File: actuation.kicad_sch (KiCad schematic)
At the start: 23 parts

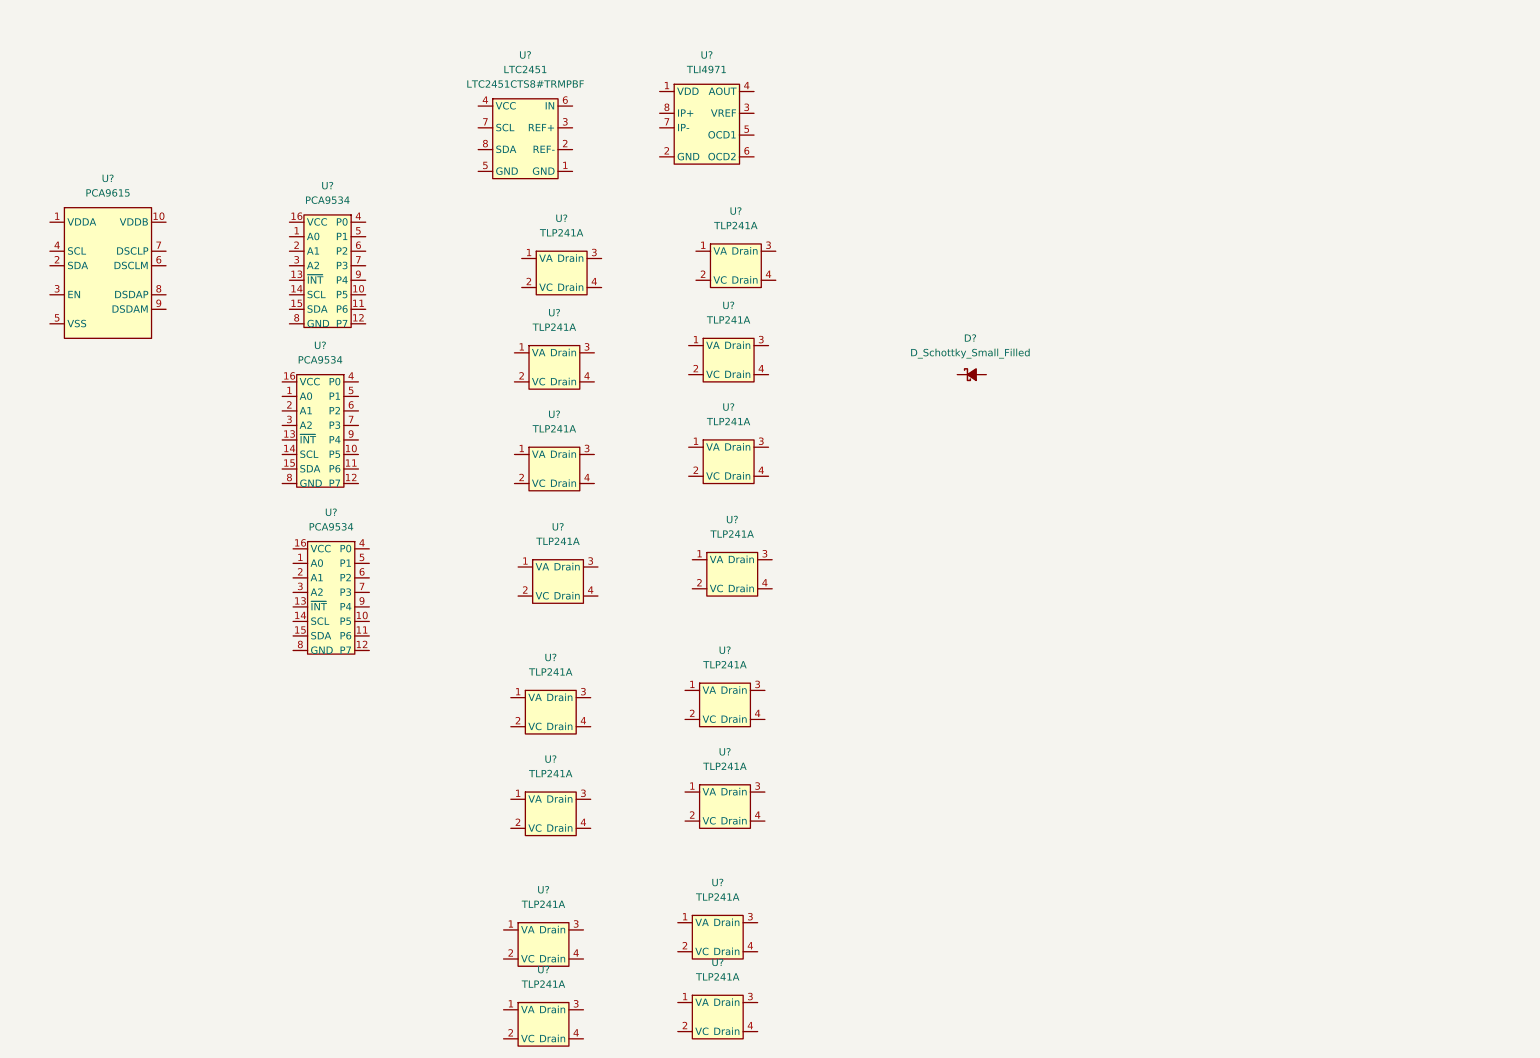
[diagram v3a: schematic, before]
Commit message: Worked on schematic, symbol placement weird
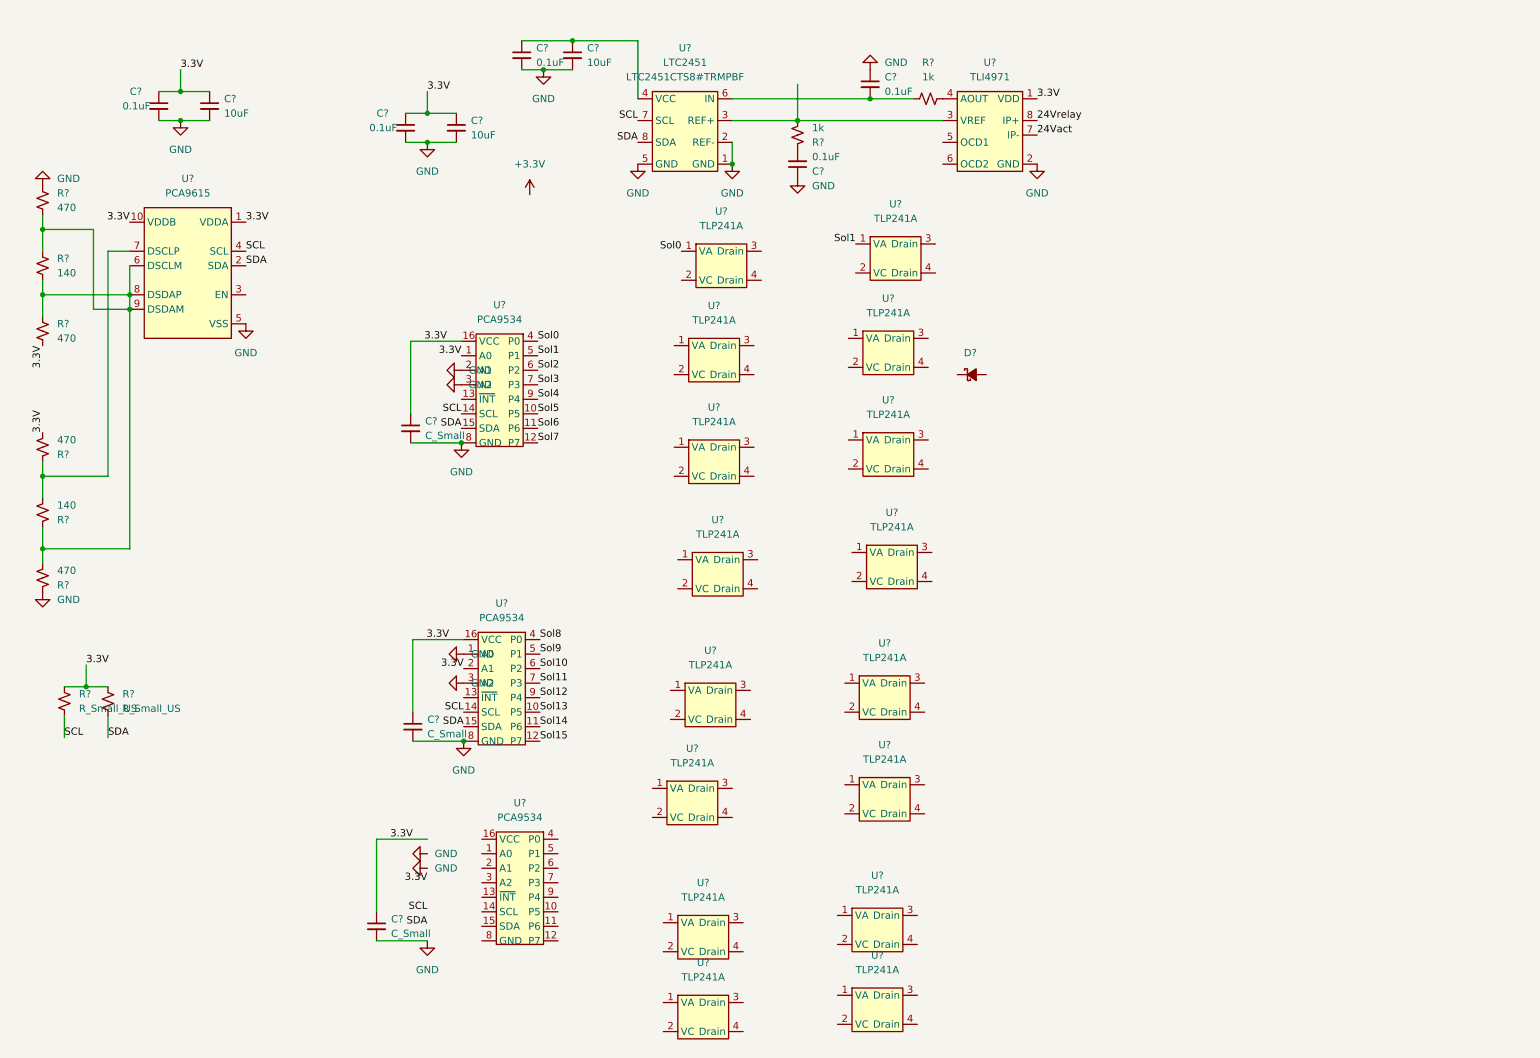
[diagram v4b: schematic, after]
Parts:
- removed U? (x2): PCA9534, Package_SO:TSSOP-16_4.4x5mm_P0.65mm, symbol actuation:PCA9534
- added C? (x3): 10uF, symbol Device:C_Small
- added C? (x5): 0.1uF, symbol Device:C_Small
- added C? (x3): C_Small, symbol Device:C_Small
- added R? (x4): 470, symbol Device:R_Small_US
- added R? (x2): 140, symbol Device:R_Small_US
- added R? (x2): 1k, symbol Device:R_Small_US
- added R? (x2): R_Small_US, symbol Device:R_Small_US
- added U? (x2): PCA9534, Package_SO:TSSOP-16_4.4x5mm_P0.65mm, symbol actuation:PCA9534
- D?: MPN (none) -> B2100A-13-F
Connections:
- net GND: now reaches U?.1 (GND)
- net GND: now also U?.2 (A1), U?.2 (GND), U?.2 (REF-), U?.3 (A2), U?.5 (GND), U?.5 (VSS), U?.8 (GND), C?.1, C?.1, C?.2, C?.2, C?.2, C?.2, C?.2, C?.2, C?.2, C?.2, C?.2, R?.2, R?.2, U?.1 (A0), U?.3 (A2), U?.8 (GND)
- net at U?.3 (REF+): now also U?.3 (VREF), R?.1
- net at U?.4 (VCC): now also C?.1, C?.1
- net at U?.6 (IN): now also C?.2, R?.1
- net SCL: now reaches U?.7 (SCL)
- net SCL: now also U?.14 (SCL), U?.4 (SCL), R?.2, U?.14 (SCL)
- net SDA: now reaches U?.8 (SDA)
- net SDA: now also U?.15 (SDA), U?.2 (SDA), R?.2, U?.15 (SDA)
- net Sol0: now reaches U?.1 (VA)
- net Sol0: now also U?.4 (P0)
- net 3.3V: now reaches U?.1 (VDD)
- net 3.3V: now also U?.1 (A0), U?.1 (VDDA), U?.10 (VDDB), U?.16 (VCC), C?.1, C?.1, C?.1, C?.1, C?.1, C?.1, C?.1, R?.1, R?.1, R?.1, R?.1, U?.16 (VCC), U?.2 (A1)
- net at U?.4 (AOUT): now also R?.2
- net 24Vact: now reaches U?.7 (IP-)
- net 24Vrelay: now reaches U?.8 (IP+)
- net Sol5: now reaches U?.10 (P5)
- net Sol6: now reaches U?.11 (P6)
- net Sol7: now reaches U?.12 (P7)
- net Sol1: now reaches U?.5 (P1)
- net Sol1: now also U?.1 (VA)
- net Sol2: now reaches U?.6 (P2)
- net Sol3: now reaches U?.7 (P3)
- net Sol4: now reaches U?.9 (P4)
- net at U?.6 (DSCLM): now also U?.8 (DSDAP), U?.9 (DSDAM), R?.1, R?.1, R?.1, R?.2, R?.2, R?.2
- net at U?.7 (DSCLP): now also R?.1, R?.2
- new net: C?.2, R?.2
- new net Sol10: U?.6 (P2)
- new net Sol11: U?.7 (P3)
- new net Sol12: U?.9 (P4)
- new net Sol13: U?.10 (P5)
- new net Sol14: U?.11 (P6)
- new net Sol15: U?.12 (P7)
- new net Sol8: U?.4 (P0)
- new net Sol9: U?.5 (P1)
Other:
- moved on the sheet: U?

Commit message: Added more symbols to schematic
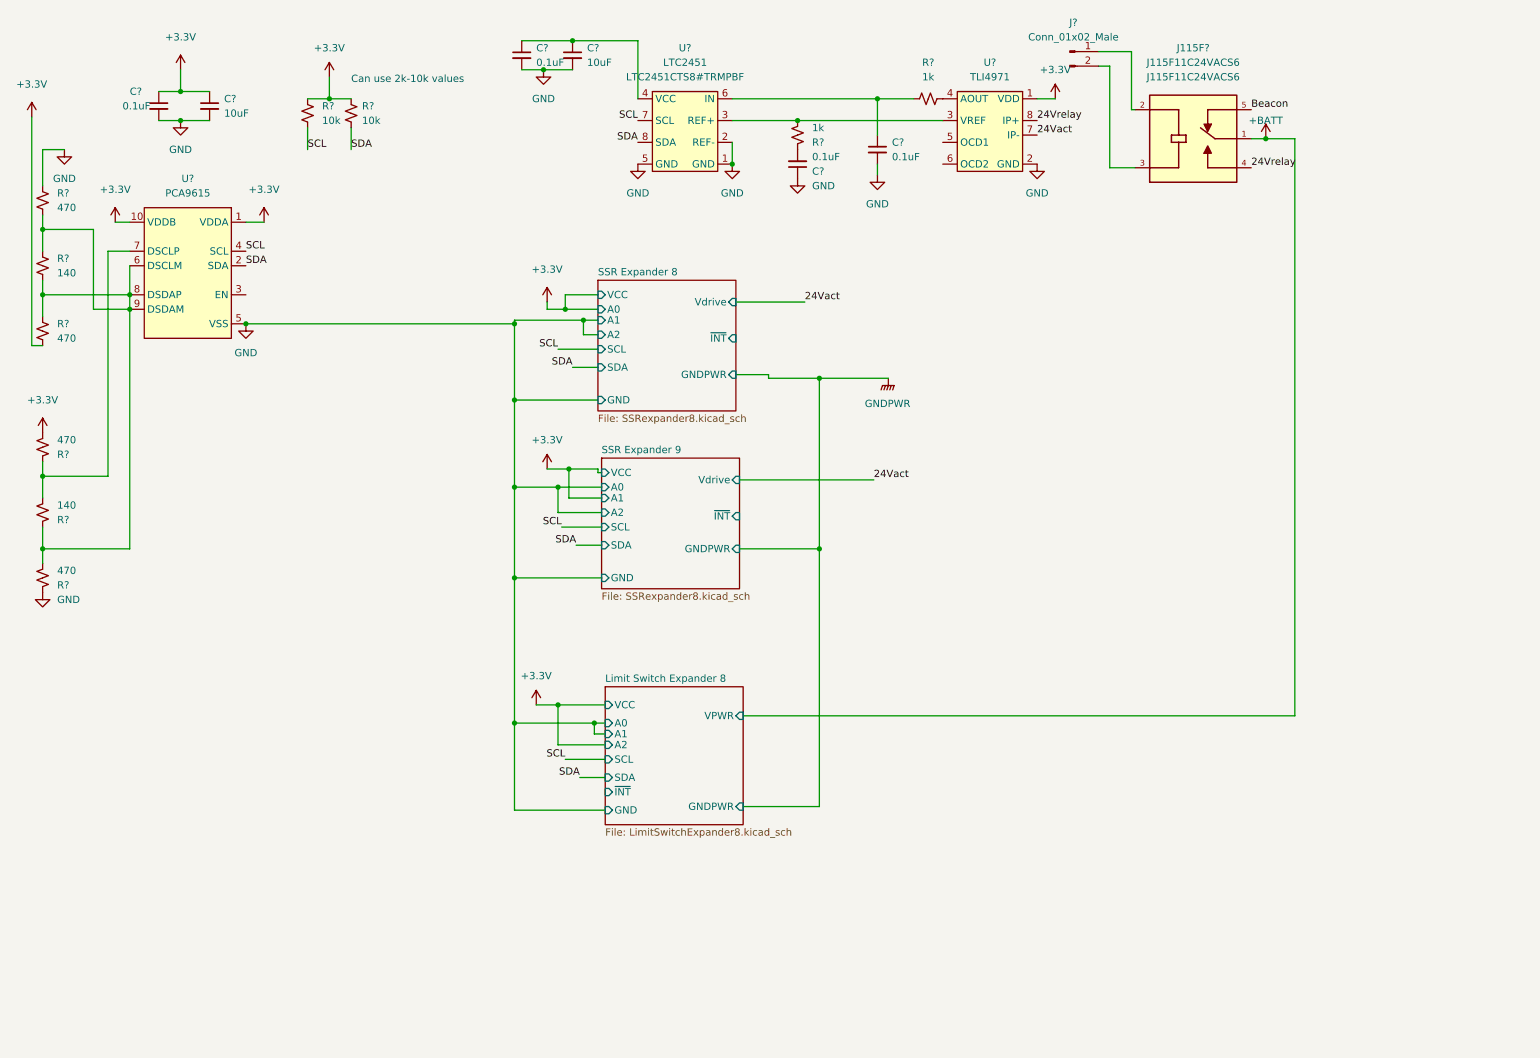
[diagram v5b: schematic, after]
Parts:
- removed C? (x2): 0.1uF, symbol Device:C_Small
- removed C?: 10uF, symbol Device:C_Small
- removed C? (x3): C_Small, symbol Device:C_Small
- removed D?: D_Schottky_Small_Filled, Diode_SMD:D_SMA, symbol Device:D_Schottky_Small_Filled
- removed U? (x16): TLP241A, symbol actuation:TLP241A
- removed U? (x3): PCA9534, Package_SO:TSSOP-16_4.4x5mm_P0.65mm, symbol actuation:PCA9534
- added C?: 0.1uF, symbol Device:C_Small
- added J115F?: J115F11C24VACS6, RELAY_J115F11C24VACS6, symbol actuation:J115F11C24VACS6
- added J?: Conn_01x02_Male, symbol Connector:Conn_01x02_Male
- R? (x2): value R_Small_US -> 10k
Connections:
- net 3.3V is gone; now on net +3.3V: C?.1, C?.1, R?.1, R?.1, R?.1, R?.1, U?.1 (VDD), U?.1 (VDDA), U?.10 (VDDB)
- net 24Vrelay: now also J115F?.4
- net GND: now also C?.2
- net at R?.1, U?.6 (IN): now also C?.1
- new net: J115F?.2, J?.1 (Pin_1)
- new net: J115F?.3, J?.2 (Pin_2)
- new net +BATT: J115F?.1
- new net Beacon: J115F?.5
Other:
- added sheet Limit Switch Expander 8 (LimitSwitchExpander8.kicad_sch)
- added sheet SSR Expander 8 (SSRexpander8.kicad_sch)
- added sheet SSR Expander 9 (SSRexpander8.kicad_sch)
- note added: "Can use 2k-10k values"
- moved on the sheet: R?

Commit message: Grid issues
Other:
- moved on the sheet: C?, J115F?, J?, R?, U?

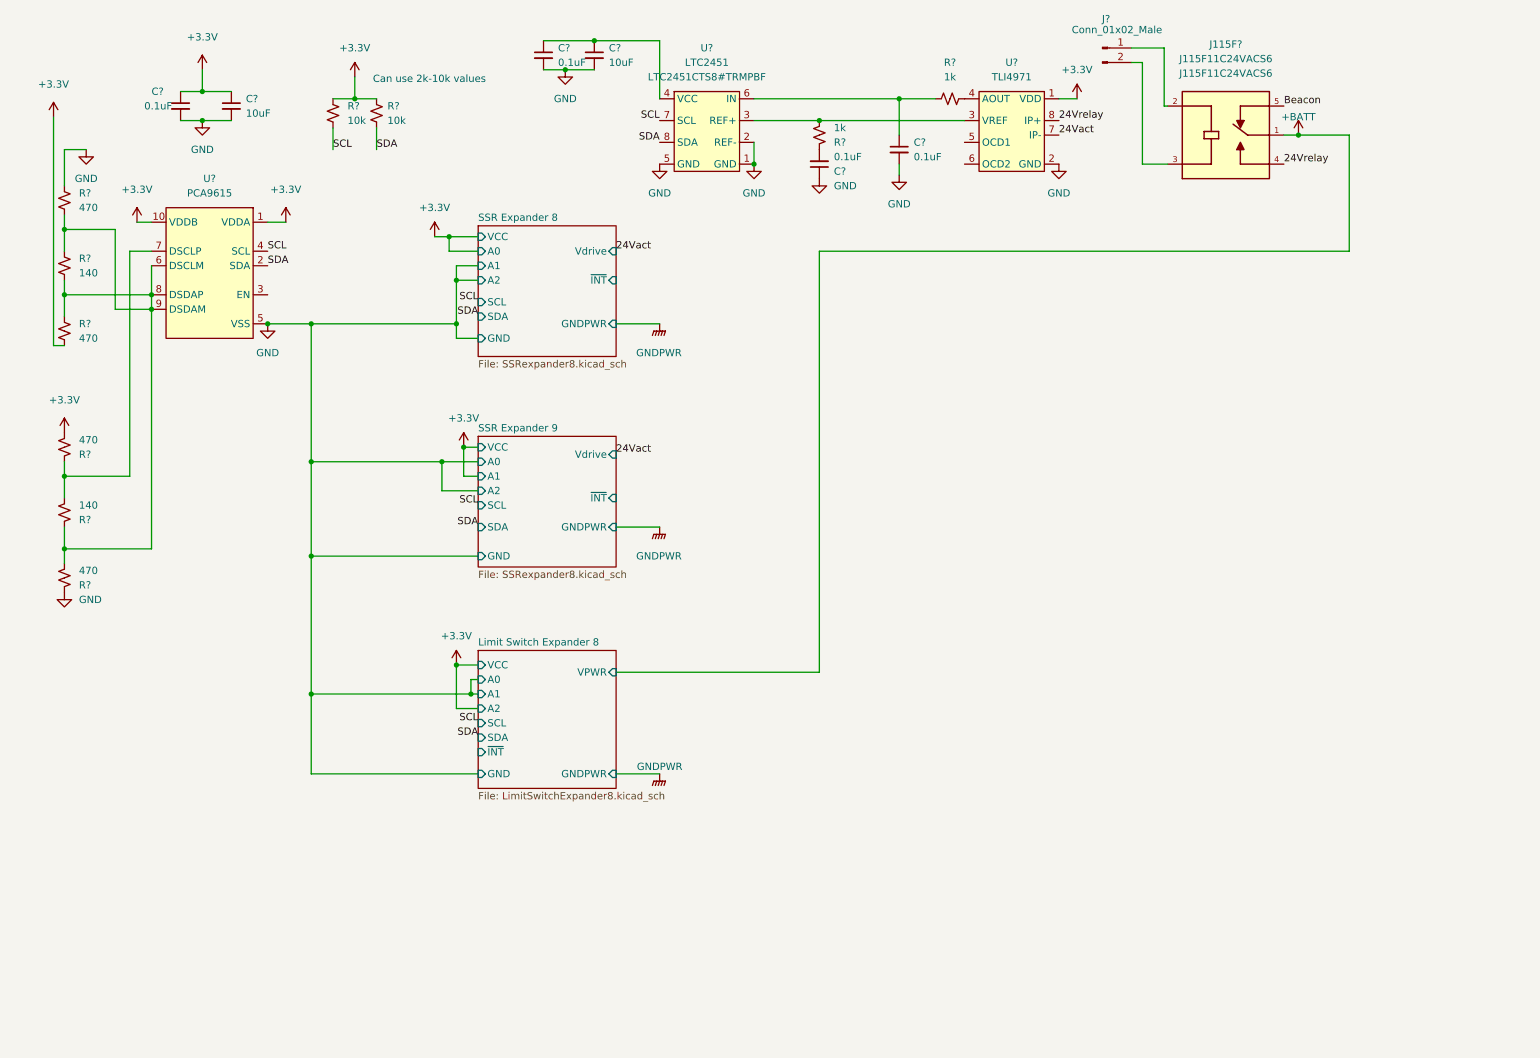
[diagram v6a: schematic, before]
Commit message: added db9 and 3.3buck
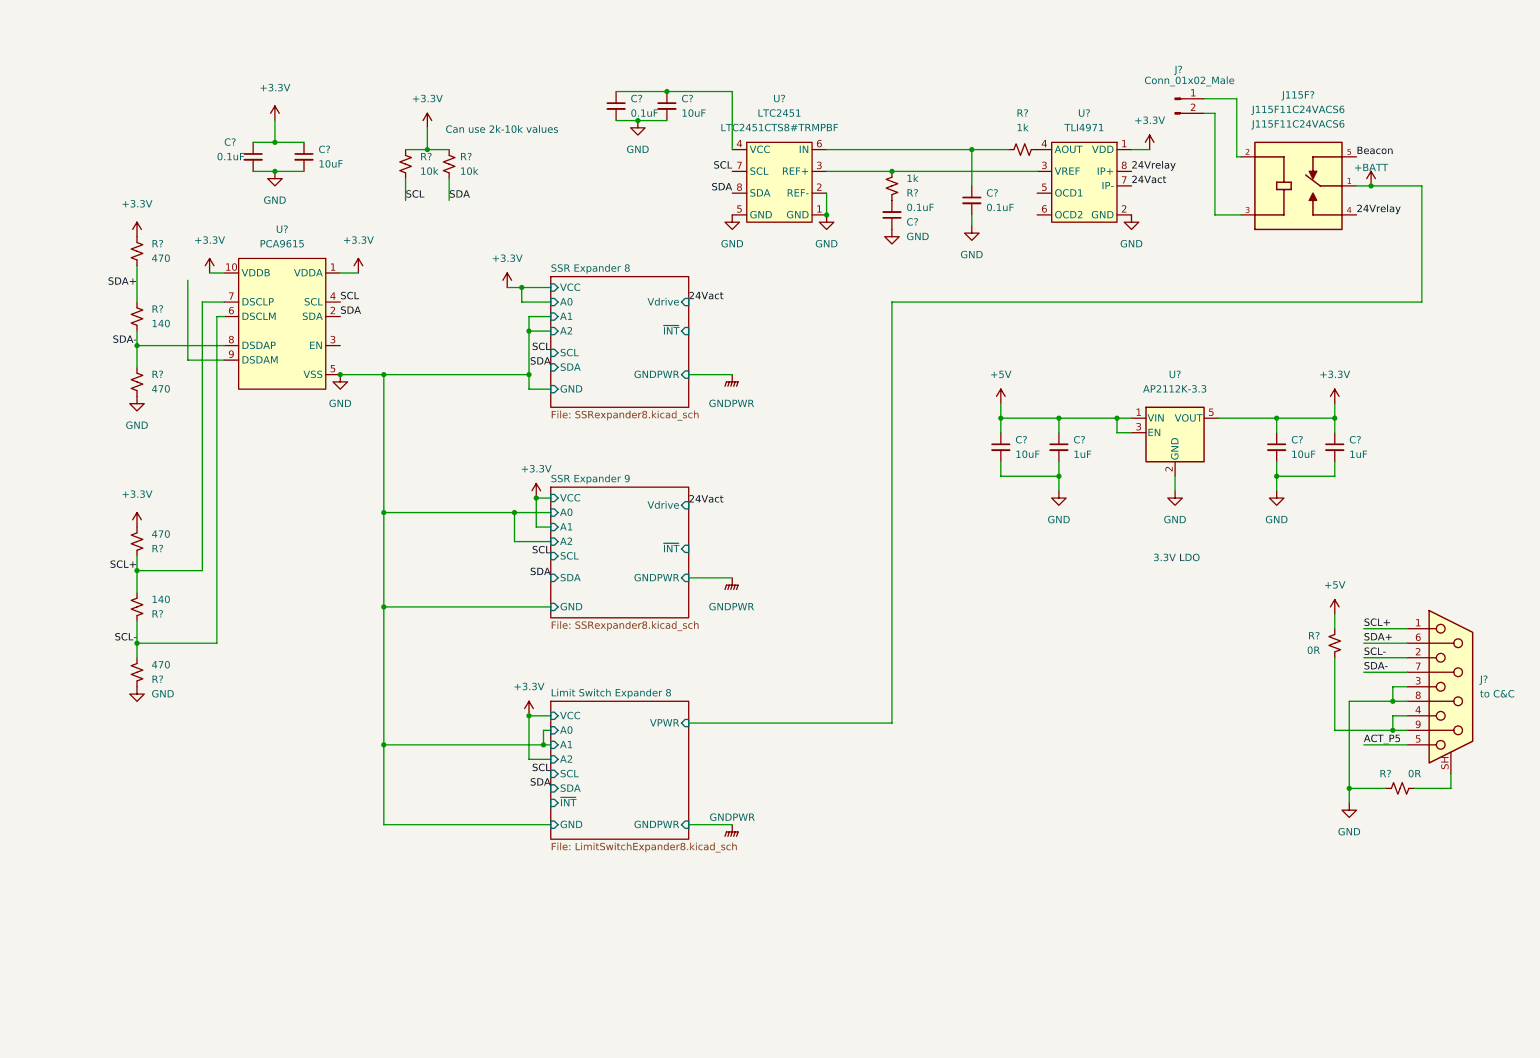
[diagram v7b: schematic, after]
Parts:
- added C? (x2): 1uF, Capacitor_SMD:C_0603_1608Metric, symbol Device:C_Small
- added C? (x2): 10uF, Capacitor_SMD:C_0805_2012Metric, symbol Device:C_Small
- added J?: to C&C, interface:182-009-213R561, symbol Connector:DB9_Female_MountingHoles
- added R? (x2): 0R, Resistor_SMD:R_0603_1608Metric, symbol Device:R_Small_US
- added U?: AP2112K-3.3, Package_TO_SOT_SMD:SOT-23-5, symbol Regulator_Linear:AP2112K-3.3
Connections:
- net +3.3V: now also R?.2, C?.1, C?.1, U?.5 (VOUT); no longer R?.1
- net GND: now also R?.1, C?.2, C?.2, C?.2, C?.2, J?.3, J?.8, R?.1, U?.2 (GND); no longer R?.2
- net SCL+: now reaches R?.1, R?.2, U?.7 (DSCLP)
- net SCL+: now also J?.1
- new net: J?.4, J?.9, R?.1
- new net: J?.SH (PAD), R?.2
- new net +5V: C?.1, C?.1, R?.2, U?.1 (VIN), U?.3 (EN)
- new net ACT_P5: J?.5
- new net SCL-: J?.2, R?.1, R?.2, U?.6 (DSCLM)
- new net SDA+: J?.6, R?.1, R?.2
- new net SDA-: J?.7, R?.1, R?.2, U?.8 (DSDAP)
- now unconnected: U?.9 (DSDAM)
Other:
- note added: "3.3V LDO"
- moved on the sheet: C?, J115F?, J?, R?, U?
